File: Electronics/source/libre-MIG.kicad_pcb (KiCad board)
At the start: 2 copper layers, 56 parts, among them J1 Conn_01x05, J10 Conn_01x03, J11 Conn_01x08, J12 Conn_01x08, J13 Conn_01x05, J14 Conn_01x03, J15 Conn_01x06, J16 Conn_01x12, J17 Conn_01x12, J18 Conn_01x03, J2 Conn_01x03, J3 Conn_01x03, J4 Conn_01x04, J4 Conn_01x05, J5 Conn_01x04, J5 Conn_01x05, J6 Conn_01x02, J7 Conn_01x02, J8 Conn_01x03, J9 Conn_01x03, P1 USB_C_Plug_USB2.0, SW1 SW_Push, SW2 SW_Push, SW3 SW_Push, U1 STM32F030C8Tx, U2 TCA9535PWR, U3 TCA9535PWR, U4 FT231XS, U5 ADP122AUJZ-3.3-R7, U6 MAX11609EEE

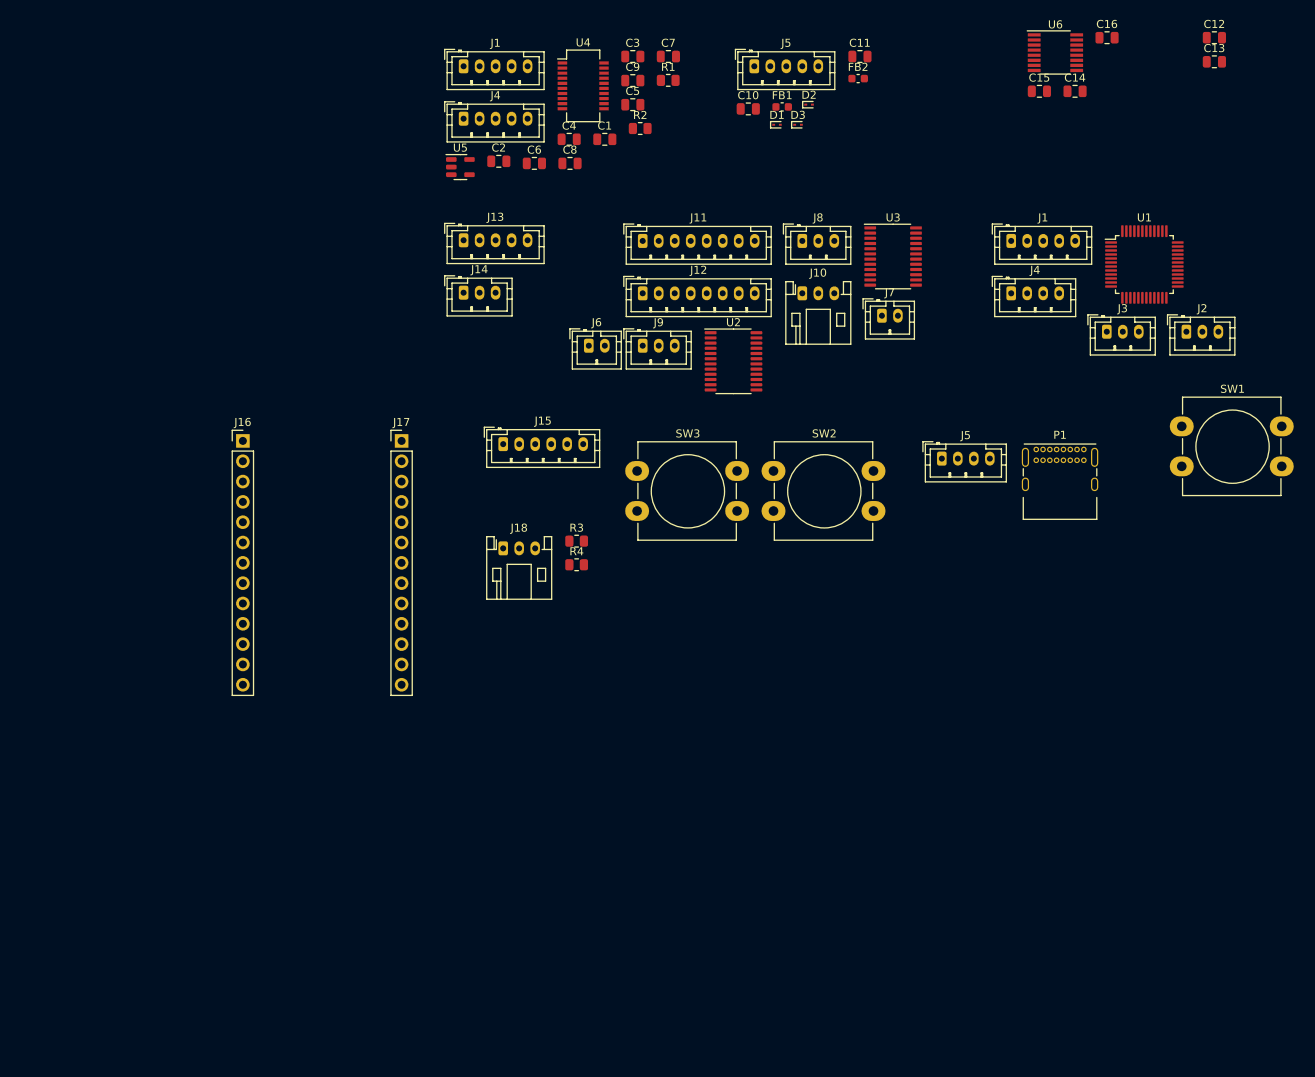
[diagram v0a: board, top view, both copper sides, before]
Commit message: started layout and finished board shapes
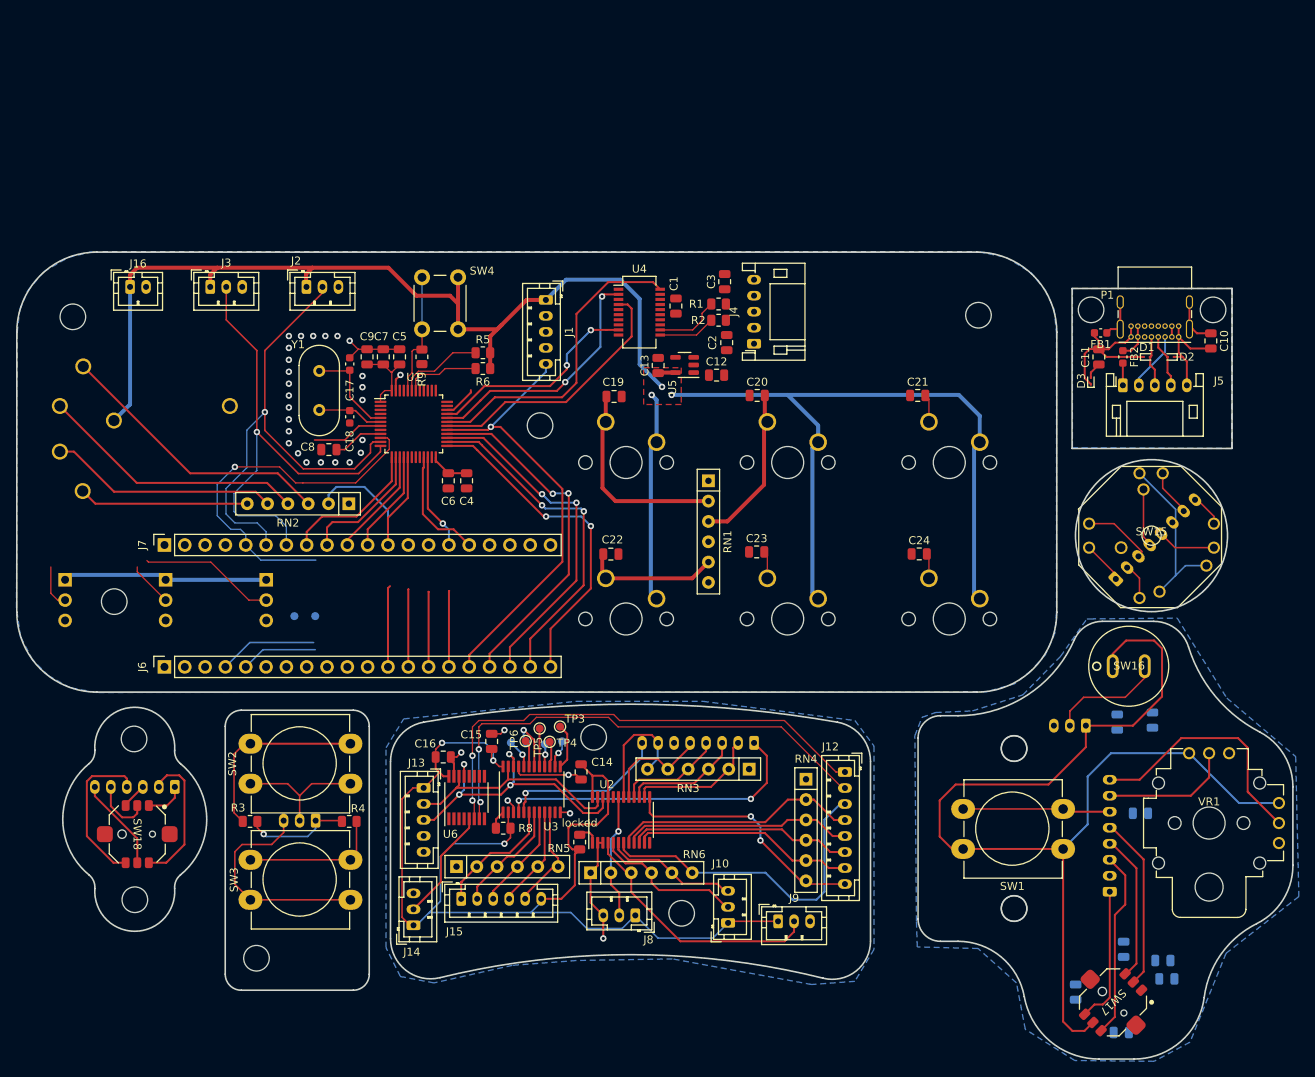
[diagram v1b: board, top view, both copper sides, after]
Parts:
- removed the J1 at (241.3, 101.6)
- removed the J4 at (172.8, 86.3)
- removed the J4 at (241.3, 108.2)
- removed the J5 at (209.2, 79.8)
- removed the J5 at (232.6, 128.8)
- added C17: 7pF, Capacitor_SMD:C_0603_1608Metric, F.Cu at (158.6, 117.0)
- added C18: 7pF, Capacitor_SMD:C_0603_1608Metric, F.Cu at (158.6, 123.6)
- added C19: 100nF, Capacitor_SMD:C_0805_2012Metric, F.Cu at (191.7, 121.0)
- added C20: 100nF, Capacitor_SMD:C_0805_2012Metric, F.Cu at (209.6, 120.9)
- added C21: 100nF, Capacitor_SMD:C_0805_2012Metric, F.Cu at (229.6, 120.9)
- added C22: 100nF, Capacitor_SMD:C_0805_2012Metric, F.Cu at (191.3, 140.7)
- added C23: 100nF, Capacitor_SMD:C_0805_2012Metric, F.Cu at (209.5, 140.5)
- added C24: 100nF, Capacitor_SMD:C_0805_2012Metric, F.Cu at (229.8, 140.7)
- added C25: 100nF, Capacitor_SMD:C_0805_2012Metric, B.Cu at (259.0, 161.5)
- added C26: 100nF, Capacitor_SMD:C_0805_2012Metric, B.Cu at (260.3, 191.5)
- added C27: 100nF, Capacitor_SMD:C_0805_2012Metric, B.Cu at (260.8, 193.8)
- added C28: 100nF, Capacitor_SMD:C_0805_2012Metric, B.Cu at (255.4, 190.1)
- added C29: 100nF, Capacitor_SMD:C_0805_2012Metric, B.Cu at (257.5, 173.1)
- added C30: 100nF, Capacitor_SMD:C_0805_2012Metric, B.Cu at (254.6, 161.7)
- added C31: 100nF, Capacitor_SMD:C_0805_2012Metric, B.Cu at (255.1, 200.5)
- added C32: 100nF, Capacitor_SMD:C_0805_2012Metric, B.Cu at (249.4, 195.5)
- added J19: Conn_01x08, Connector_JST:JST_PH_S8B-PH-K_1x08_P2.00mm_Horizontal, B.Cu at (253.6, 182.9)
- added J20: Conn_01x03, Connector_JST:JST_PH_B3B-PH-K_1x03_P2.00mm_Vertical, B.Cu at (250.6, 162.2)
- added J21: Conn_01x08, Connector_JST:JST_PH_B8B-PH-K_1x08_P2.00mm_Vertical, B.Cu at (254.4, 143.9)
- added J4: Conn_01x05, Connector_JST:JST_PH_S5B-PH-K_1x05_P2.00mm_Horizontal, F.Cu at (209.2, 114.4)
- added J5: Conn_01x05, Connector_JST:JST_PH_S5B-PH-K_1x05_P2.00mm_Horizontal, F.Cu at (255.3, 119.6)
- added R5: 3k, Resistor_SMD:R_0805_2012Metric, F.Cu at (175.3, 115.6)
- added R6: 3k, Resistor_SMD:R_0805_2012Metric, F.Cu at (175.3, 117.6)
- added R8: 10k, Resistor_SMD:R_0805_2012Metric, F.Cu at (177.8, 175.0)
- added R9: 10k, Resistor_SMD:R_0805_2012Metric, F.Cu at (167.6, 116.1)
- added REF**: MountingHole_3.2mm_M3, MountingHole:MountingHole_3.2mm_M3, F.Cu at (182.4, 124.7)
- added REF**: MountingHole_3.2mm_M3, MountingHole:MountingHole_3.2mm_M3, F.Cu at (251.5, 110.2)
- added REF**: MountingHole_3.2mm_M3, MountingHole:MountingHole_3.2mm_M3, F.Cu at (241.7, 185.0)
- added REF**: MountingHole_3.2mm_M3, MountingHole:MountingHole_3.2mm_M3, F.Cu at (124.0, 111.1)
- added REF**: MountingHole_3.2mm_M3, MountingHole:MountingHole_3.2mm_M3, F.Cu at (131.8, 184.0)
- added REF**: MountingHole_3.2mm_M3, MountingHole:MountingHole_3.2mm_M3, F.Cu at (189.1, 163.6)
- added REF**: MountingHole_3.2mm_M3, MountingHole:MountingHole_3.2mm_M3, F.Cu at (129.2, 146.7)
- added REF**: MountingHole_3.2mm_M3, MountingHole:MountingHole_3.2mm_M3, F.Cu at (266.7, 110.1)
- added REF**: MountingHole_3.2mm_M3, MountingHole:MountingHole_3.2mm_M3, F.Cu at (241.7, 165.0)
- added REF**: MountingHole_3.2mm_M3, MountingHole:MountingHole_3.2mm_M3, F.Cu at (131.7, 163.9)
- added REF**: MountingHole_3.2mm_M3, MountingHole:MountingHole_3.2mm_M3, F.Cu at (147.0, 191.3)
- added REF**: MountingHole_3.2mm_M3, MountingHole:MountingHole_3.2mm_M3, F.Cu at (237.2, 110.9)
- added REF**: MountingHole_3.2mm_M3, MountingHole:MountingHole_3.2mm_M3, F.Cu at (200.1, 185.6)
- added RN1: R_Network05, Resistor_THT:R_Array_SIP6, F.Cu at (203.5, 131.6)
- added RN2: R_Network05, Resistor_THT:R_Array_SIP6, F.Cu at (158.5, 134.4)
- added RN3: R_Network05, Resistor_THT:R_Array_SIP6, F.Cu at (208.5, 167.6)
- added RN4: R_Network05, Resistor_THT:R_Array_SIP6, F.Cu at (215.6, 168.9)
- added RN5: R_Network05, Resistor_THT:R_Array_SIP6, F.Cu at (172.0, 179.8)
- added RN6: R_Network05, Resistor_THT:R_Array_SIP6, F.Cu at (188.7, 180.6)
- added SW10: SW_Push, Button_Switch_Keyboard:SW_Cherry_MX_1.00u_PCB, B.Cu at (231.0, 124.2)
- added SW11: SW_Push, Button_Switch_Keyboard:SW_Cherry_MX_1.00u_PCB, B.Cu at (190.6, 143.8)
- added SW12: SW_Push, Button_Switch_Keyboard:SW_Cherry_MX_1.00u_PCB, B.Cu at (210.8, 143.8)
- added SW13: SW_Push, Button_Switch_Keyboard:SW_Cherry_MX_1.00u_PCB, B.Cu at (231.0, 143.8)
- added SW14: SW_Coded, Personal:KC14A10.001NPS, B.Cu at (133.0, 125.1)
- added SW15: RKJXV1220, Personal:RKJXT1F, F.Cu at (258.8, 138.4)
- added SW16: SW_Push, Personal:PS1024AL, F.Cu at (256.0, 154.8)
- added SW17: SKRHABE010, Personal:SKRHABE010, F.Cu at (254.0, 196.8)
- added SW18: SKRHABE010, Personal:SKRHABE010, F.Cu at (132.1, 175.8)
- added SW4: SW_Push, Button_Switch_THT:SW_PUSH_6mm, F.Cu at (172.2, 106.1)
- added SW5: SW_SPDT, Connector_PinHeader_2.54mm:PinHeader_1x03_P2.54mm_Vertical, B.Cu at (135.6, 144.0)
- added SW6: SW_SPDT, Connector_PinHeader_2.54mm:PinHeader_1x03_P2.54mm_Vertical, B.Cu at (148.2, 144.0)
- added SW7: SW_SPDT, Connector_PinHeader_2.54mm:PinHeader_1x03_P2.54mm_Vertical, B.Cu at (123.0, 144.0)
- added SW8: SW_Push, Button_Switch_Keyboard:SW_Cherry_MX_1.00u_PCB, B.Cu at (190.6, 124.2)
- added SW9: SW_Push, Button_Switch_Keyboard:SW_Cherry_MX_1.00u_PCB, B.Cu at (210.8, 124.2)
- added TP1: TestPoint, TestPoint:TestPoint_Pad_D1.0mm, B.Cu at (151.7, 148.5)
- added TP10: TestPoint, TestPoint:TestPoint_Pad_D1.0mm, B.Cu at (178.8, 164.3)
- added TP2: TestPoint, TestPoint:TestPoint_Pad_D1.0mm, B.Cu at (154.3, 148.5)
- added TP3: TestPoint, TestPoint:TestPoint_Pad_D1.0mm, F.Cu at (184.9, 162.3)
- added TP4: TestPoint, TestPoint:TestPoint_Pad_D1.0mm, F.Cu at (183.6, 164.2)
- added TP5: TestPoint, TestPoint:TestPoint_Pad_D1.0mm, F.Cu at (182.4, 162.5)
- added TP6: TestPoint, TestPoint:TestPoint_Pad_D1.0mm, F.Cu at (180.6, 164.1)
- added TP7: TestPoint, TestPoint:TestPoint_Pad_D1.0mm, B.Cu at (185.2, 164.1)
- added TP8: TestPoint, TestPoint:TestPoint_Pad_D1.0mm, B.Cu at (183.0, 164.5)
- added TP9: TestPoint, TestPoint:TestPoint_Pad_D1.0mm, B.Cu at (180.8, 164.3)
- added VR1: Joystick_Pot, Personal:RKJXV1220, F.Cu at (266.0, 174.4)
- added Y1: ABL-32.000MHZ-B2, Crystal:Crystal_HC49-U_Vertical, F.Cu at (154.8, 122.7)
- added locked: 10k, Resistor_SMD:R_0805_2012Metric, F.Cu at (187.4, 176.7)
- J10: footprint Connector_JST:JST_PH_S3B-PH-K_1x03_P2.00mm_Horizontal -> Connector_JST:JST_PH_B3B-PH-K_1x03_P2.00mm_Vertical
- J11: footprint Connector_JST:JST_PH_B8B-PH-K_1x08_P2.00mm_Vertical -> Connector_JST:JST_PH_S8B-PH-K_1x08_P2.00mm_Horizontal; moved to B.Cu
- J16: value Conn_01x12 -> Conn_01x02; footprint Connector_PinHeader_2.54mm:PinHeader_1x13_P2.54mm_Vertical -> Connector_JST:JST_PH_B2B-PH-K_1x02_P2.00mm_Vertical
- J17: value Conn_01x12 -> Conn_01x06; footprint Connector_PinHeader_2.54mm:PinHeader_1x13_P2.54mm_Vertical -> Connector_JST:JST_PH_S6B-PH-K_1x06_P2.00mm_Horizontal; moved to B.Cu
- J18: moved to B.Cu
- J6, J7: value Conn_01x02 -> Conn_01x20; footprint Connector_JST:JST_PH_B2B-PH-K_1x02_P2.00mm_Vertical -> Connector_PinSocket_2.54mm:PinSocket_1x20_P2.54mm_Vertical
- U6: value MAX11609EEE -> MAX11615EEE
- moved C16 122.3 mm to (170.3, 166.1), turned to 180 degrees
- moved U6 118.7 mm to (173.2, 171.2), turned to 90 degrees
- moved J3 112.2 mm to (141.2, 107.3)
- moved J2 110.1 mm to (153.2, 107.3)
- moved C15 106.3 mm to (176.4, 164.2), turned to -90 degrees
- moved C14 105.1 mm to (187.5, 168.0), turned to 90 degrees
- moved J7 94.2 mm to (135.5, 139.6), turned to 90 degrees
- moved U1 93.5 mm to (166.6, 124.5)
- moved J8 86.9 mm to (194.3, 185.9), turned to 180 degrees
- moved U3 80.5 mm to (181.4, 170.2), turned to 90 degrees
- moved J14 79.3 mm to (166.6, 187.1), turned to 90 degrees
- moved J10 79.2 mm to (205.9, 186.8), turned to 90 degrees
- moved C13 79.2 mm to (197.2, 117.2), turned to 90 degrees
- moved C12 75.2 mm to (204.5, 118.4)
- moved J9 73.9 mm to (212.2, 186.6)
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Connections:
- C14 pad 2: unconnected-(C14-Pad2) -> +3V3
- C15 pad 2: unconnected-(C15-Pad2) -> +3V3
- J11 pad 2: /IO Controller/EncodeB -> /IO Controller/DirU1
- J11 pad 3: /IO Controller/DirC1 -> /IO Controller/DirR1
- J11 pad 4: /IO Controller/DirR1 -> /IO Controller/DirC1
- J11 pad 6: /IO Controller/DirU1 -> GND
- J11 pad 8: GND -> /IO Controller/EncodeB
- J16 pad 1: /MCU/TxD -> +3V3
- J16 pad 2: /MCU/RxD -> GND
- J17 pad 1: +5V -> /Trigger/SideA
- J17 pad 2: GND -> /Trigger/SideB
- J17 pad 3: /MCU/NRST -> /Trigger/SideC
- J17 pad 4: +3V3 -> /Trigger/SideD
- J17 pad 5: unconnected-(J17-Pad5) -> /Trigger/SideCenter
- J17 pad 6: /MCU/PitchIn -> +3V3
- J7 pad 1: +3V3 -> unconnected-(J7-Pad1)
- J7 pad 2: GND -> unconnected-(J7-Pad2)
- SW1 pad 1: unconnected-(SW1-Pad1) -> +3V3
- SW1 pad 2: unconnected-(SW1-Pad2) -> /Face Plate/CenterButt
- U1 pad 10: unconnected-(U1-Pad10) -> /MCU/SW1
- U1 pad 13: unconnected-(U1-Pad13) -> /MCU/ADC3
- U1 pad 14: unconnected-(U1-Pad14) -> /MCU/Togg1
- U1 pad 15: unconnected-(U1-Pad15) -> /MCU/Togg2
- U1 pad 16: unconnected-(U1-Pad16) -> /MCU/Togg3
- U1 pad 17: unconnected-(U1-Pad17) -> /MCU/SW6
- U1 pad 20: unconnected-(U1-Pad20) -> GND
- U1 pad 21: unconnected-(U1-Pad21) -> /MCU/Rot1
- U1 pad 22: unconnected-(U1-Pad22) -> /MCU/Rot2
- U1 pad 25: unconnected-(U1-Pad25) -> /MCU/Rot3
- U1 pad 26: unconnected-(U1-Pad26) -> /MCU/Rot4
- U1 pad 27: unconnected-(U1-Pad27) -> /MCU/SW2
- U1 pad 28: unconnected-(U1-Pad28) -> /MCU/SW3
- U1 pad 29: unconnected-(U1-Pad29) -> /MCU/EN
- U1 pad 34: unconnected-(U1-Pad34) -> /MCU/SWDIO
- U1 pad 37: unconnected-(U1-Pad37) -> /MCU/SWCLK
- U1 pad 42: unconnected-(U1-Pad42) -> /MCU/SCL
- U1 pad 43: unconnected-(U1-Pad43) -> /MCU/SDA
- U1 pad 44: unconnected-(U1-Pad44) -> Net-(R9-Pad2)
- U1 pad 45: unconnected-(U1-Pad45) -> /MCU/SW4
- U1 pad 46: unconnected-(U1-Pad46) -> /MCU/SW5
- U1 pad 5: unconnected-(U1-Pad5) -> Net-(C17-Pad2)
- U1 pad 6: unconnected-(U1-Pad6) -> Net-(C18-Pad2)
- U2 pad 1: unconnected-(U2-Pad1) -> Net-(R7-Pad1)
- U2 pad 14: /IO Controller/DirC1 -> /IO Controller/DirU1
- U2 pad 15: /IO Controller/DirL1 -> /IO Controller/DirR1
- U2 pad 16: /IO Controller/DirR1 -> /IO Controller/DirC1
- U2 pad 17: /IO Controller/DirU1 -> /IO Controller/DirL1
- U2 pad 21: GND -> +3V3
- U2 pad 22: unconnected-(U2-Pad22) -> /IO Controller/SCL
- U2 pad 23: unconnected-(U2-Pad23) -> /IO Controller/SDA
- U2 pad 3: +3V3 -> GND
- U3 pad 1: unconnected-(U3-Pad1) -> Net-(R8-Pad1)
- U3 pad 13: unconnected-(U3-Pad13) -> /IO Controller/IN_xtra1
- U3 pad 14: unconnected-(U3-Pad14) -> /IO Controller/IN_xtra2
- U3 pad 15: unconnected-(U3-Pad15) -> /IO Controller/IN_xtra3
- U3 pad 16: unconnected-(U3-Pad16) -> /IO Controller/IN_xtra4
- U3 pad 17: unconnected-(U3-Pad17) -> /IO Controller/IN_xtra5
- U3 pad 18: unconnected-(U3-Pad18) -> /IO Controller/IN_xtra6
- U3 pad 19: unconnected-(U3-Pad19) -> /IO Controller/IN_xtra7
- U3 pad 20: unconnected-(U3-Pad20) -> /IO Controller/IN_xtra8
- U3 pad 22: unconnected-(U3-Pad22) -> /IO Controller/SCL
- U3 pad 23: unconnected-(U3-Pad23) -> /IO Controller/SDA
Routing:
- net +3V3: track 0.00 -> 586.1 mm, vias 0 -> 7
- net GND: track 0.00 -> 97.4 mm, vias 0 -> 32
- net /MCU/SW1: track 0.00 -> 72.6 mm, vias 0 -> 1
- net /MCU/Rot3: track 0.00 -> 70.5 mm, vias 0 -> 2
- net /MCU/Rot4: track 0.00 -> 64.1 mm, vias 0 -> 2
- net /MCU/SW2: track 0.00 -> 63.8 mm, vias 0 -> 2
- net /IO Controller/Axis1: track 0.00 -> 61.8 mm, vias 0 -> 2
- net /MCU/PitchIn: track 0.00 -> 61.7 mm, vias 0 -> 1
- net /IO Controller/Axis2: track 0.00 -> 61.5 mm, vias 0 -> 2
- net /MCU/YawIn: track 0.00 -> 60.0 mm, vias 0 -> 1
- net /MCU/EN: track 0.00 -> 55.6 mm, vias 0 -> 1
- net /MCU/Rot1: track 0.00 -> 49.8 mm
- net /MCU/RxD: track 0.00 -> 48.7 mm
- net /MCU/SW3: track 0.00 -> 47.6 mm, vias 0 -> 2
- net /MCU/Rot2: track 0.00 -> 45.6 mm, vias 0 -> 1
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- added copper zone on F.Cu, net +3V3
- added copper zone on B.Cu, net GND
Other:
- board outline added: 159.5 x 100.9 mm

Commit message: Finished first layout of all boards
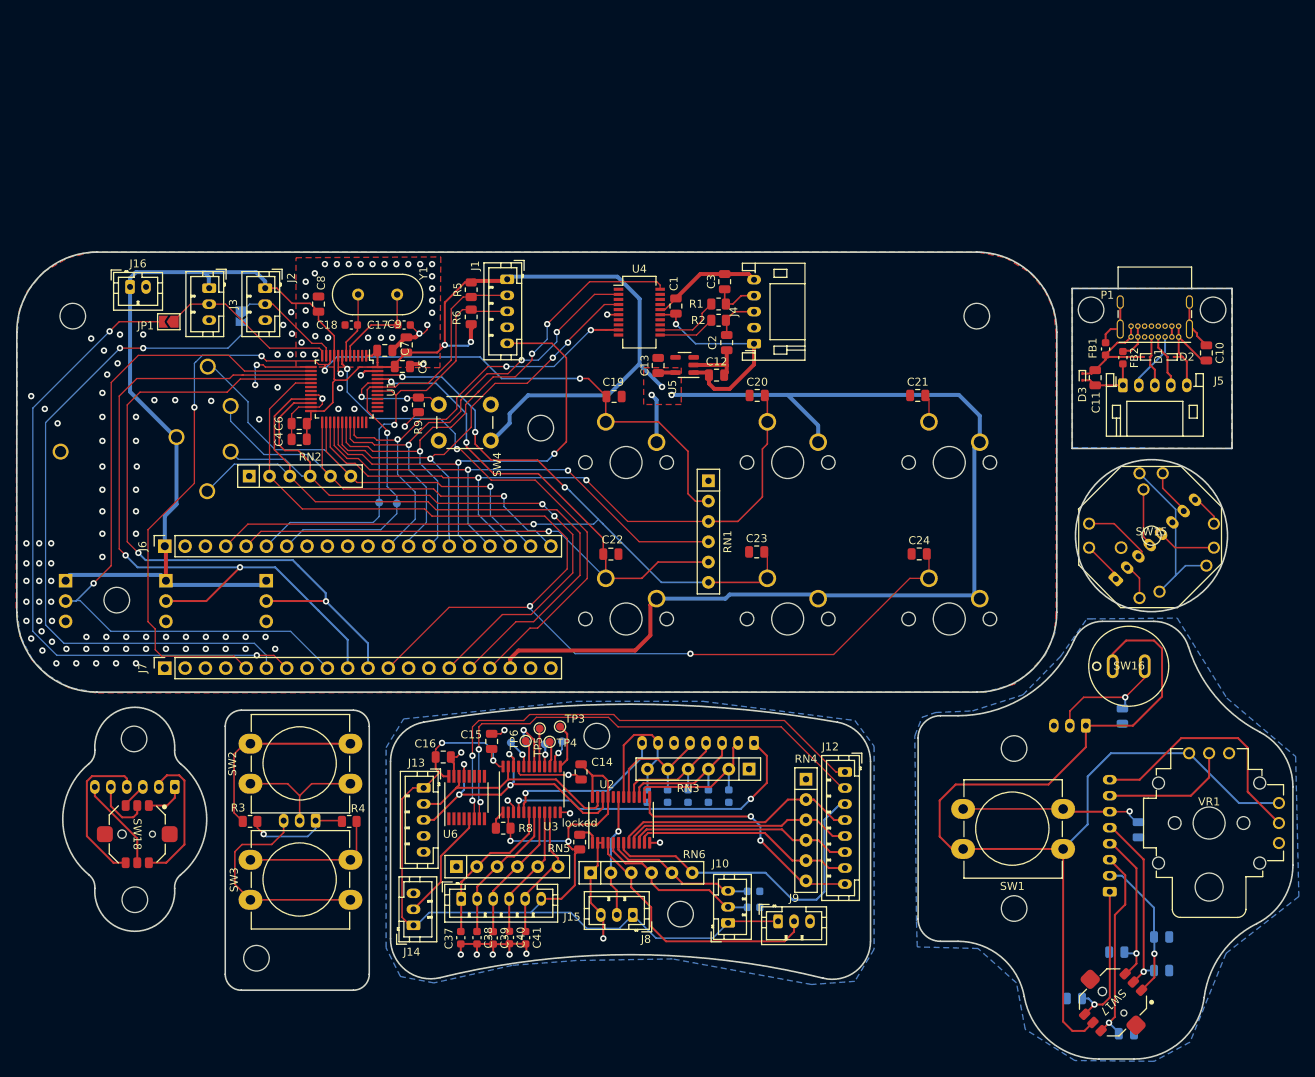
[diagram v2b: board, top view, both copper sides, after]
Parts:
- added C33: 100nF, Capacitor_SMD:C_0603_1608Metric, B.Cu at (203.4, 171.0)
- added C34: 100nF, Capacitor_SMD:C_0603_1608Metric, B.Cu at (198.3, 171.0)
- added C35: 100nF, Capacitor_SMD:C_0603_1608Metric, B.Cu at (195.8, 171.0)
- added C36: 100nF, Capacitor_SMD:C_0603_1608Metric, B.Cu at (206.0, 171.0)
- added C37: 100nF, Capacitor_SMD:C_0603_1608Metric, F.Cu at (172.5, 188.7)
- added C38: 100nF, Capacitor_SMD:C_0603_1608Metric, F.Cu at (174.5, 188.7)
- added C39: 100nF, Capacitor_SMD:C_0603_1608Metric, F.Cu at (176.6, 188.7)
- added C40: 100nF, Capacitor_SMD:C_0603_1608Metric, F.Cu at (178.6, 188.7)
- added C41: 100nF, Capacitor_SMD:C_0603_1608Metric, F.Cu at (180.6, 188.7)
- added C42: 100nF, Capacitor_SMD:C_0603_1608Metric, B.Cu at (209.1, 184.9)
- added C43: 100nF, Capacitor_SMD:C_0603_1608Metric, B.Cu at (209.1, 182.9)
- added JP1: Jumper_2_Open, Jumper:SolderJumper-2_P1.3mm_Open_TrianglePad1.0x1.5mm, F.Cu at (136.0, 111.7)
- added JP2: Jumper_2_Open, Jumper:SolderJumper-2_P1.3mm_Open_TrianglePad1.0x1.5mm, B.Cu at (145.1, 111.0)
- C25: footprint Capacitor_SMD:C_0805_2012Metric -> Capacitor_SMD:C_0603_1608Metric
- moved C25 58.8 mm to (200.9, 171.0)
- moved SW7 25.1 mm to (148.2, 144.1)
- moved C4 21.6 mm to (152.3, 126.4), turned to 180 degrees
- moved SW4 20.8 mm to (176.2, 126.5), turned to 180 degrees
- moved C6 20.0 mm to (152.3, 124.4), turned to 180 degrees
- moved TP1 19.0 mm to (164.5, 134.4), turned to 0 degrees
- moved C8 18.2 mm to (154.7, 109.5), turned to 90 degrees
- moved TP2 16.3 mm to (162.3, 134.3), turned to 0 degrees
- moved J7 15.4 mm to (135.5, 155.0)
- moved Y1 15.2 mm to (159.7, 108.3), turned to 0 degrees
- moved J6 15.1 mm to (135.5, 139.8)
- moved RN2 12.9 mm to (146.1, 131.0), turned to 0 degrees
- moved SW6 12.5 mm to (135.6, 144.1)
- moved SW5 12.5 mm to (123.1, 144.1)
- moved C18 11.5 mm to (158.8, 112.1), turned to 0 degrees
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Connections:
- C25 pad 1: /Face Plate/BigRed -> /IO Controller/DirC1
- J6 pad 3: +5V -> unconnected-(J6-Pad3)
- J7 pad 6: /MCU/PitchIn -> /MCU/PitchIn2
- J7 pad 7: /MCU/YawIn -> /MCU/YawIn2
- J7 pad 8: /MCU/ADC3 -> unconnected-(J7-Pad8)
- TP1 pad 1: /IO Controller/SCL -> /MCU/SDA
- TP2 pad 1: /IO Controller/SDA -> /MCU/SCL
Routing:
- net /MCU/SW6: track 30.0 -> 146.7 mm, vias 0 -> 2
- net /MCU/SW5: track 16.3 -> 114.1 mm, vias 0 -> 4
- net /MCU/PitchIn2: track 0.00 -> 86.7 mm, vias 0 -> 2
- net /MCU/YawIn2: track 0.00 -> 82.3 mm, vias 0 -> 2
- net /MCU/SW4: track 26.5 -> 105.8 mm, vias 0 -> 3
- net /MCU/Togg1: track 22.0 -> 92.5 mm, vias 0 -> 1
- net /MCU/Togg3: track 18.3 -> 88.0 mm, vias 0 -> 2
- net /MCU/Togg2: track 30.7 -> 92.1 mm, vias 0 -> 2
- net /MCU/SW1: track 72.6 -> 131.9 mm, vias 1 -> 4
- net +3V3: track 586.1 -> 645.0 mm, vias 7 -> 10
- net /MCU/NRST: track 8.98 -> 65.6 mm, vias 0 -> 2
- net GND: track 97.4 -> 145.6 mm, vias 32 -> 129
- net /MCU/SDA: track 10.9 -> 58.4 mm, vias 0 -> 1
- net /MCU/PitchIn: track 61.7 -> 14.1 mm, vias 1 -> 0
- net /MCU/SCL: track 9.49 -> 57.0 mm, vias 0 -> 1
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- added copper zone on F.Cu, net GND
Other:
- outline, holes or cut-outs redrawn
